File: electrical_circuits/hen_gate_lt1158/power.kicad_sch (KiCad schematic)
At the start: 13 parts, among them IC2 IFX007TAUMA1, IC3 IFX007TAUMA1, J1 MOTOR OUTPUT

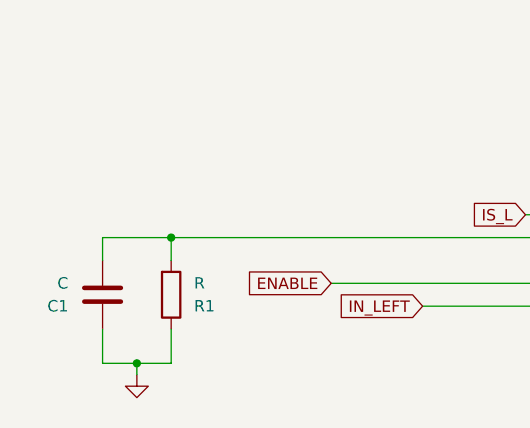
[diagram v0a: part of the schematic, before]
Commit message: Added 8-bit uC to hen_gate_lt1158 project.
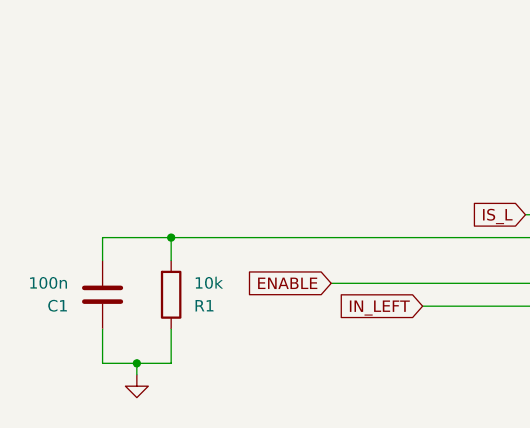
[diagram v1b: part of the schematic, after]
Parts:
- C1: value C -> 100n
- R1: value R -> 10k
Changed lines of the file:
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@@
 			)
 		)
-		(property "Value" "R"
+		(property "Value" "10k"
 			(at 49.53 129.5401 0)
 			(effects
@@
 			)
 		)
-		(property "Value" "C"
+		(property "Value" "100n"
 			(at 35.56 129.5401 0)
 			(effects
